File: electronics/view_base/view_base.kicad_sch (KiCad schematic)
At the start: 107 parts, among them J1 BLDC, J2 USB_C_Receptacle_USB2.0, J3 LCD, J4 A, J5 B, Q1 MMBT4403, Q2 UMH3N, U1 MT6701-CT, U2 T-Micro32_Plus, U3 CH340C, U4 HX711, U5 TMC6300, U6 AP2114HA-3.3, U7 SN74LV1T34DBV, U8 VEML7700, U9 TS1117BCW33_RPG

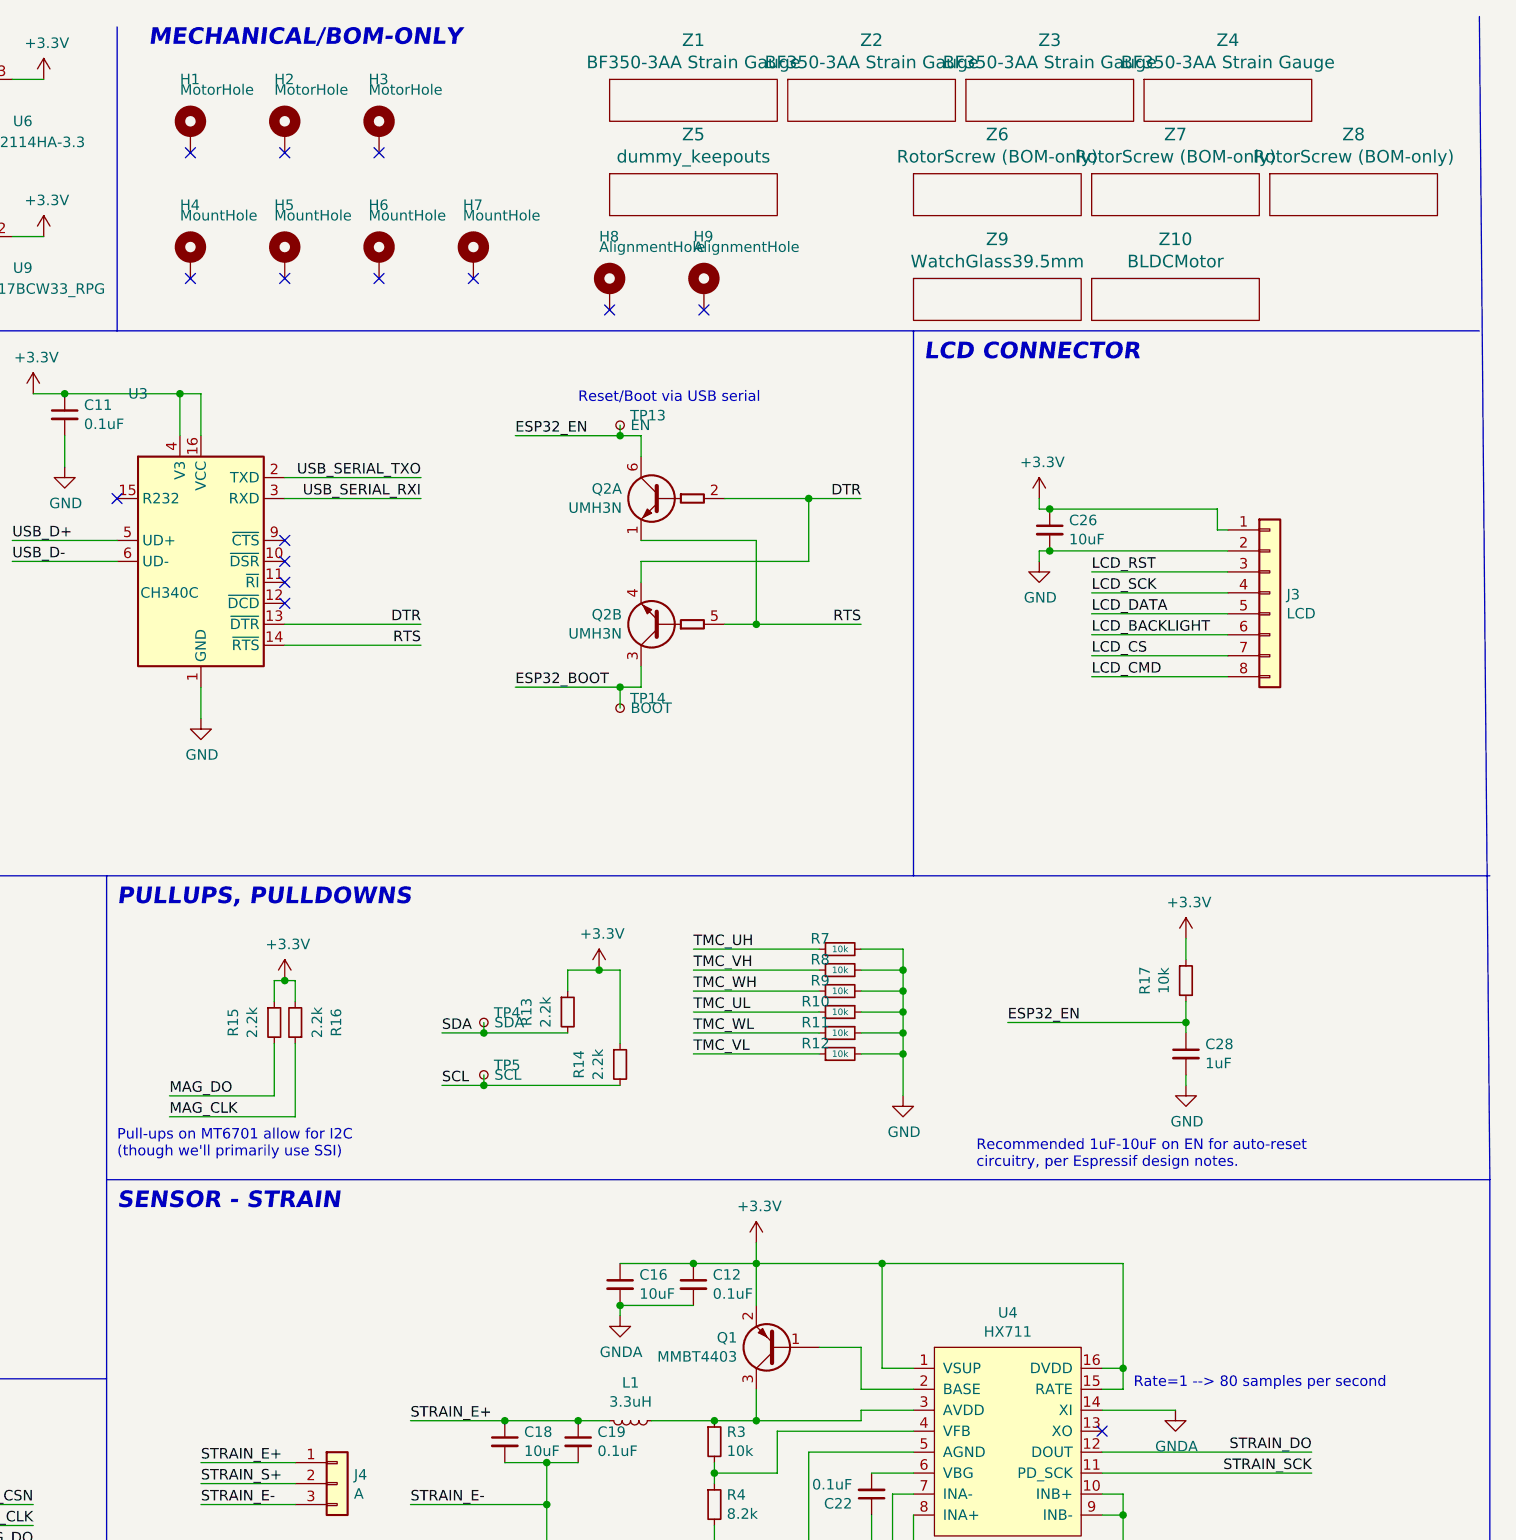
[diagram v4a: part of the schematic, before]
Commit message: Use 2512 SMD resistors in place of strain gauges (#104)
As suggested in https://github.com/scottbez1/smartknob/issues/24#issuecomment-1073540944 and inspired by https://github.com/IvDm/Z-probe-on-smd-resistors-2512, this adds 4x 330 ohm 2512 SMD resistors to the back to act as strain gauges, rather than requiring discrete strain gauges to be glued and wired up.

Also applies a few changes I accidentally had pending locally:
- Custom footprints for the 2 3.3v LDO options to clarify the pinout options
![image](https://user-images.githubusercontent.com/414890/204078474-8327e8ed-78b5-4fe3-a91d-9c20fe54fcbc.png)
- some BOM note updates

Fixes #24
Closes #33
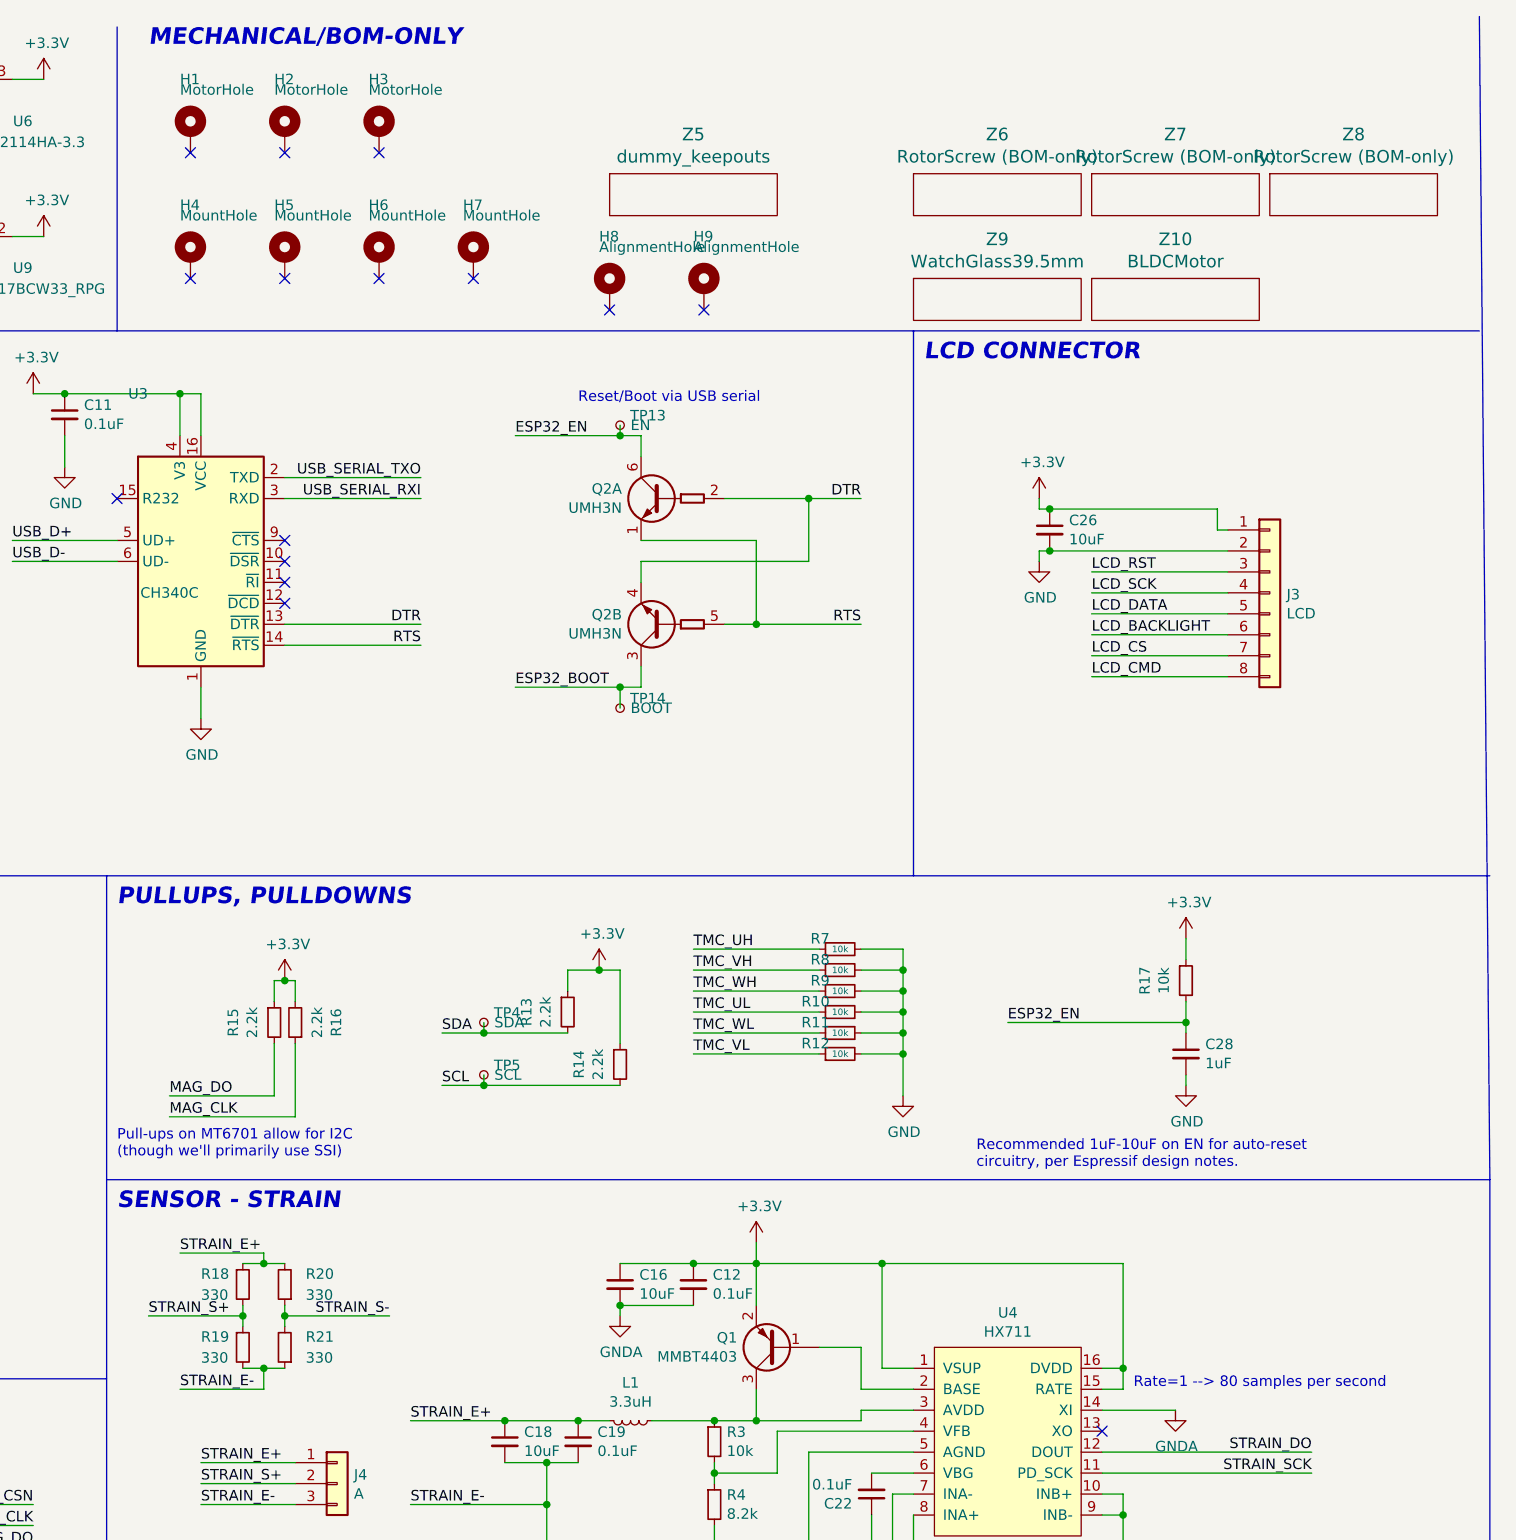
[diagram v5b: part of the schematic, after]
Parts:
- removed Z1, Z2, Z3, Z4: BF350-3AA Strain Gauge, strain:BF350-3AA, symbol no_pin:no_pin
- added R18, R19, R20, R21: 330, Resistor_SMD:R_2512_6332Metric, symbol Device:R_Small
- U6: footprint Package_TO_SOT_SMD:SOT-223-3_TabPin2 -> Modified:SOT-223-3_TabPin2_InGndOut
- U9: footprint Package_TO_SOT_SMD:SOT-223-3_TabPin2 -> Modified:SOT-223-3_TabPin2_GndOutIn
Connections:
- net GNDA: now also R19.2, R21.1
- net STRAIN_E+: now also R18.1, R20.2
- net STRAIN_S+: now also R18.2, R19.1
- net STRAIN_S-: now also R20.1, R21.2

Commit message: BOM - Replace discontinued C2922480 with C15850
Fixes #139 - thanks @lorhof1 and @Wilgelmy
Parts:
- C10, C16, C18, C24, C26, C9: LCSC C2922480 -> C15850
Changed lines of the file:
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@@
       (effects (font (size 1.27 1.27)) hide)
     )
-    (property "LCSC" "C2922480" (id 4) (at 158.75 184.15 0)
+    (property "LCSC" "C15850" (id 4) (at 158.75 184.15 0)
       (effects (font (size 1.27 1.27)) hide)
     )
@@
       (effects (font (size 1.27 1.27)) hide)
     )
-    (property "LCSC" "C2922480" (id 4) (at 22.86 33.02 0)
+    (property "LCSC" "C15850" (id 4) (at 22.86 33.02 0)
       (effects (font (size 1.27 1.27)) hide)
     )
@@
       (effects (font (size 1.27 1.27)) hide)
     )
-    (property "LCSC" "C2922480" (id 4) (at 36.83 33.02 0)
+    (property "LCSC" "C15850" (id 4) (at 36.83 33.02 0)
       (effects (font (size 1.27 1.27)) hide)
     )
@@
       (effects (font (size 1.27 1.27)) hide)
     )
-    (property "LCSC" "C2922480" (id 4) (at 172.72 165.1 0)
+    (property "LCSC" "C15850" (id 4) (at 172.72 165.1 0)
       (effects (font (size 1.27 1.27)) hide)
     )
@@
       (effects (font (size 1.27 1.27)) hide)
     )
-    (property "LCSC" "C2922480" (id 4) (at 317.5 30.48 0)
+    (property "LCSC" "C15850" (id 4) (at 317.5 30.48 0)
       (effects (font (size 1.27 1.27)) hide)
     )
@@
       (effects (font (size 1.27 1.27)) hide)
     )
-    (property "LCSC" "C2922480" (id 4) (at 224.79 73.66 0)
-      (effects (font (size 1.27 1.27)) hide)
-    )
+    (property "LCSC" "C15850" (id 4) (at 224.79 73.66 0)
+      (effects (font (size 1.27 1.27)) hide)
+    )
